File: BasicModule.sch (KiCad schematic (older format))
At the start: 12 parts, among them P1 CONN_01X03, Q1 Q_NPN_BCE, SW1 SW_Push_Dual

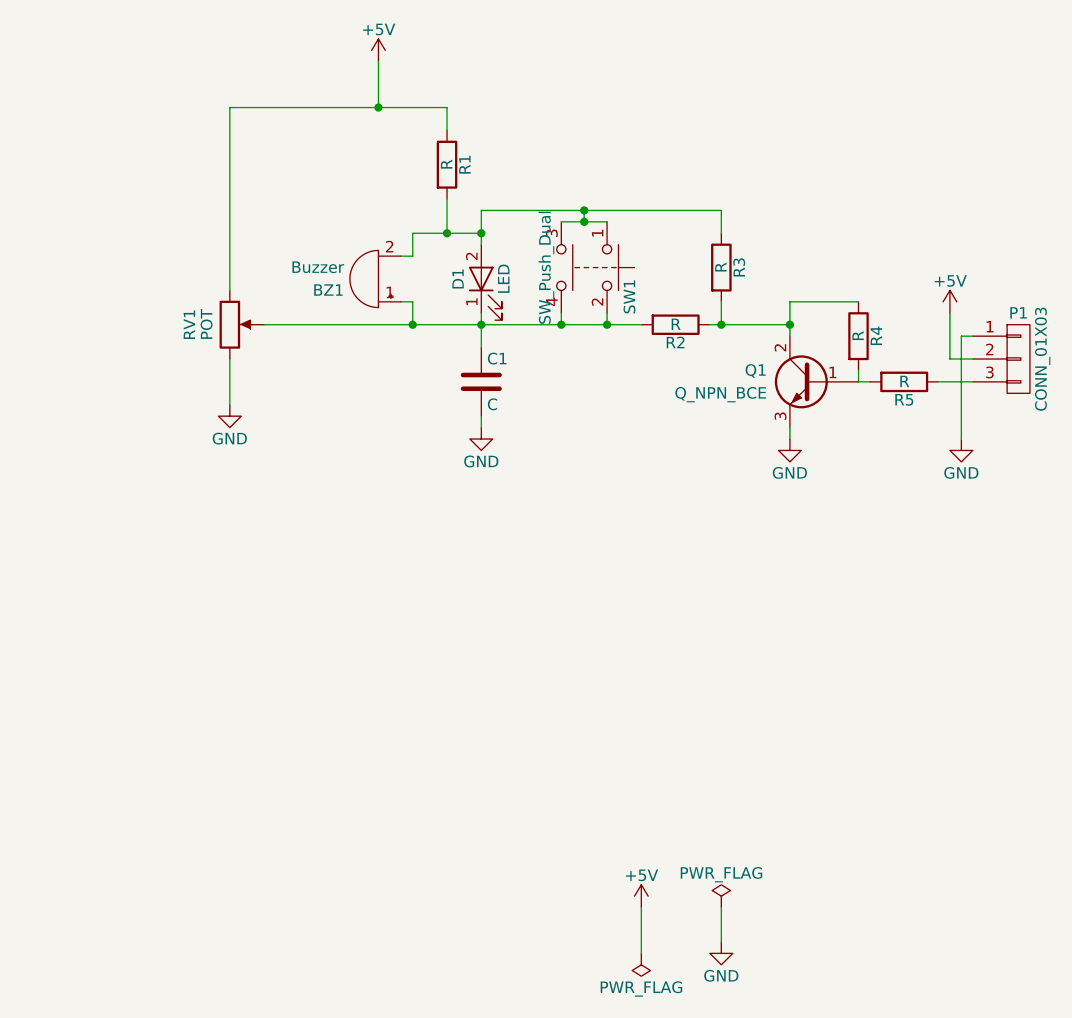
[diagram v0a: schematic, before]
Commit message: Se decide implementar el modulo solo para leds, buzzers y potenciometro
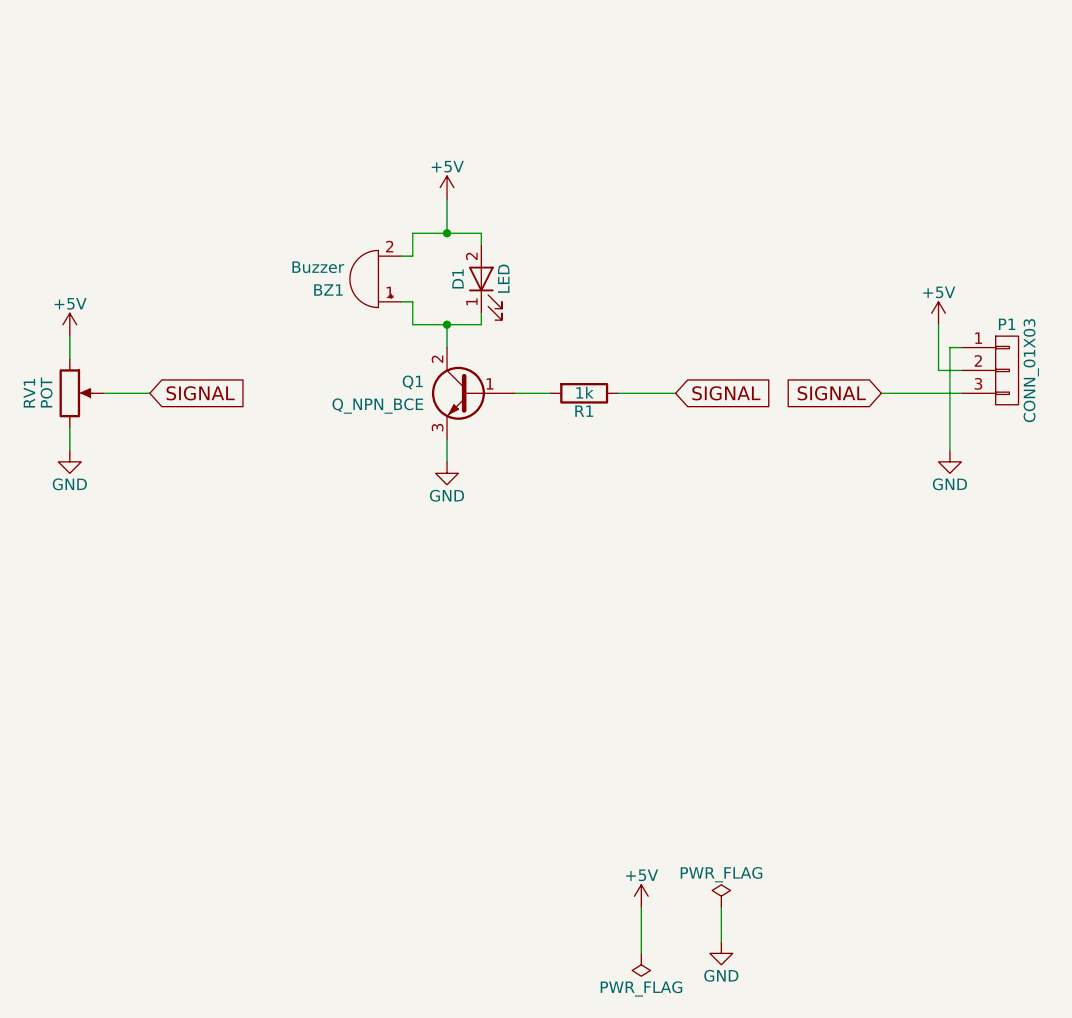
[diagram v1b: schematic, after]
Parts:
- removed C1: C, symbol C
- removed R2, R3, R4, R5: R, symbol R
- removed SW1: SW_Push_Dual, symbol SW_Push_Dual
- BZ1: footprint (none) -> Buzzers_Beepers:Buzzer_12x9.5RM7.6
- D1: footprint (none) -> LEDs:LED-5MM
- P1: footprint (none) -> Connectors_JST:JST_PH_S3B-PH-K_03x2.00mm_Angled
- Q1: footprint (none) -> TO_SOT_Packages_SMD:SOT-23
- R1: value R -> 1k; footprint (none) -> Resistors_SMD:R_0805
- RV1: footprint (none) -> w_pth_resistors:trimmer_alps-rk09k1130ah1
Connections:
- net +5V: now also BZ1.2 (+), D1.2 (A); no longer R1.1
- net at BZ1.1 (-), D1.1 (K): now also Q1.2 (C); no longer RV1.2
- net at Q1.1 (B): now also R1.2
- net SIGNAL: now reaches P1.3 (P3)
- net SIGNAL: now also R1.1, RV1.2
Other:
- moved on the sheet: P1, Q1, R1, RV1

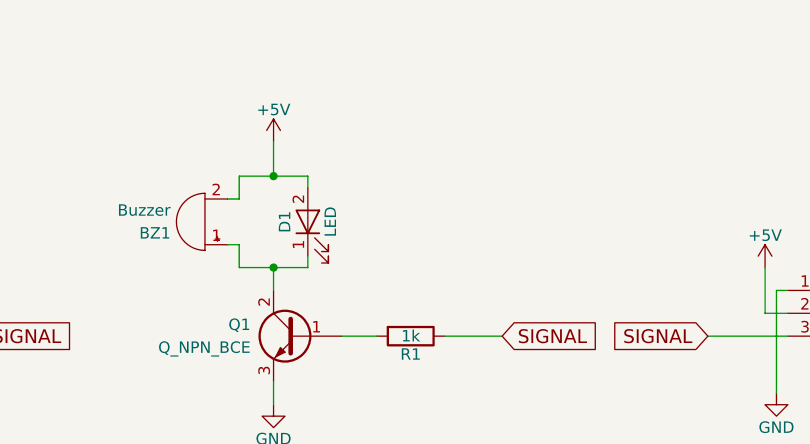
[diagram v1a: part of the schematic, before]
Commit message: Led piraña añadido al modulo
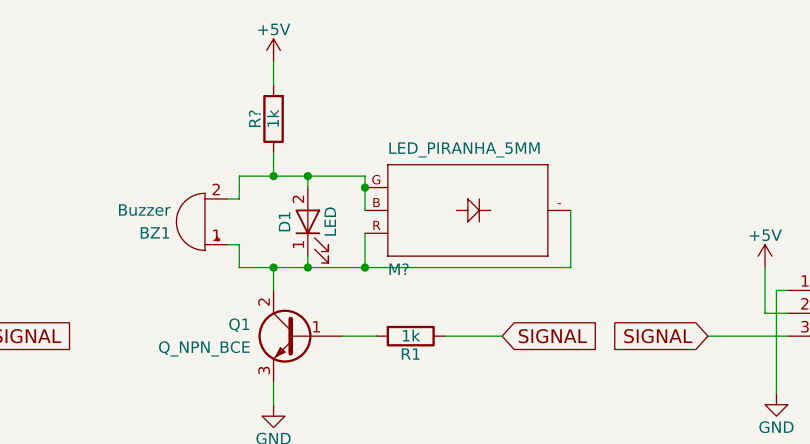
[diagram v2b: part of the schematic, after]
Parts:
- added M?: LED_PIRANHA_5MM, LED_PIRANHA_5MM, symbol LED_PIRANHA_5MM
- added R?: 1k, Resistors_SMD:R_0805, symbol R
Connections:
- net +5V: now also R?.2; no longer BZ1.2 (+), D1.2 (A)
- net at BZ1.1 (-), D1.1 (K), Q1.2 (C): now also M?.- (C), M?.R (RED)
- new net: BZ1.2 (+), D1.2 (A), M?.B (BLU), M?.G (GRN), R?.1
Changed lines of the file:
@@
 LIBS:рэс-49
 LIBS:тпг-1
+LIBS:SparkFun-LED
 LIBS:BasicModule-cache
 EELAYER 25 0
@@
 L +5V #PWR02
 U 1 1 5907709F
-P 5350 3950
-F 0 "#PWR02" H 5350 3800 50  0001 C CNN
-F 1 "+5V" H 5350 4090 50  0000 C CNN
-F 2 "" H 5350 3950 50  0001 C CNN
-F 3 "" H 5350 3950 50  0001 C CNN
-	1    5350 3950
+P 5350 3600
+F 0 "#PWR02" H 5350 3450 50  0001 C CNN
+F 1 "+5V" H 5350 3740 50  0000 C CNN
+F 2 "" H 5350 3600 50  0001 C CNN
+F 3 "" H 5350 3600 50  0001 C CNN
+	1    5350 3600
 	1    0    0    -1
 $EndComp
@@
 	5200 4200 5200 4100
 $Comp
-L +5V #PWR05
+L +5V #PWR03
 U 1 1 59078247
 P 7500 4500
-F 0 "#PWR05" H 7500 4350 50  0001 C CNN
+F 0 "#PWR03" H 7500 4350 50  0001 C CNN
 F 1 "+5V" H 7500 4640 50  0000 C CNN
 F 2 "" H 7500 4500 50  0001 C CNN
@@
 	7500 4700 7500 4500
 $Comp
-L GND #PWR06
+L GND #PWR04
 U 1 1 59078352
 P 7550 5050
-F 0 "#PWR06" H 7550 4800 50  0001 C CNN
+F 0 "#PWR04" H 7550 4800 50  0001 C CNN
 F 1 "GND" H 7550 4900 50  0000 C CNN
 F 2 "" H 7550 5050 50  0001 C CNN
@@
 	7550 4600 7550 5050
 $Comp
-L PWR_FLAG #FLG07
+L PWR_FLAG #FLG05
 U 1 1 590785A3
 P 6550 7050
-F 0 "#FLG07" H 6550 7125 50  0001 C CNN
+F 0 "#FLG05" H 6550 7125 50  0001 C CNN
 F 1 "PWR_FLAG" H 6550 7200 50  0000 C CNN
 F 2 "" H 6550 7050 50  0001 C CNN
@@
 $EndComp
 $Comp
-L GND #PWR08
+L GND #PWR06
 U 1 1 590786A5
 P 6550 7200
-F 0 "#PWR08" H 6550 6950 50  0001 C CNN
+F 0 "#PWR06" H 6550 6950 50  0001 C CNN
 F 1 "GND" H 6550 7050 50  0000 C CNN
 F 2 "" H 6550 7200 50  0001 C CNN
@@
 	6550 7050 6550 7200
 $Comp
-L +5V #PWR09
+L +5V #PWR07
 U 1 1 59078AD8
 P 6200 7050
-F 0 "#PWR09" H 6200 6900 50  0001 C CNN
+F 0 "#PWR07" H 6200 6900 50  0001 C CNN
 F 1 "+5V" H 6200 7190 50  0000 C CNN
 F 2 "" H 6200 7050 50  0001 C CNN
@@
 $EndComp
 $Comp
-L PWR_FLAG #FLG010
+L PWR_FLAG #FLG08
 U 1 1 59078BDF
 P 6200 7250
-F 0 "#FLG010" H 6200 7325 50  0001 C CNN
+F 0 "#FLG08" H 6200 7325 50  0001 C CNN
 F 1 "PWR_FLAG" H 6200 7400 50  0000 C CNN
 F 2 "" H 6200 7250 50  0001 C CNN
@@
 	5500 4100 5500 4150
 Wire Wire Line
-	5200 4500 5500 4500
+	5200 4500 6650 4500
 Wire Wire Line
 	5500 4500 5500 4450
@@
 	5350 5000 5350 5100
 Wire Wire Line
-	5200 4100 5500 4100
-Wire Wire Line
-	5350 3950 5350 4100
+	5200 4100 5750 4100
 Connection ~ 5350 4100
 Wire Wire Line
@@
 SIGNAL
 $Comp
-L +5V #PWR?
+L +5V #PWR09
 U 1 1 59109538
 P 3700 4550
-F 0 "#PWR?" H 3700 4400 50  0001 C CNN
+F 0 "#PWR09" H 3700 4400 50  0001 C CNN
 F 1 "+5V" H 3700 4690 50  0000 C CNN
 F 2 "" H 3700 4550 50  0001 C CNN
@@
 $EndComp
 $Comp
-L GND #PWR?
+L GND #PWR010
 U 1 1 591095BB
 P 3700 5050
-F 0 "#PWR?" H 3700 4800 50  0001 C CNN
+F 0 "#PWR010" H 3700 4800 50  0001 C CNN
 F 1 "GND" H 3700 4900 50  0000 C CNN
 F 2 "" H 3700 5050 50  0001 C CNN
@@
 Wire Wire Line
 	3700 4950 3700 5050
+$Comp
+L LED_PIRANHA_5MM M?
+U 1 1 5910A2C3
+P 6150 4250
+F 0 "M?" H 5850 4480 50  0000 L BNN
+F 1 "LED_PIRANHA_5MM" H 5850 3950 50  0000 L BNN
+F 2 "LED_PIRANHA_5MM" H 6180 4400 20  0001 C CNN
+F 3 "" H 6150 4250 60  0001 C CNN
+	1    6150 4250
+	1    0    0    1
+$EndComp
+$Comp
+L R R?
+U 1 1 5910A539
+P 5350 3850
+F 0 "R?" V 5430 3850 50  0000 C CNN
+F 1 "1k" V 5350 3850 50  0000 C CNN
+F 2 "Resistors_SMD:R_0805" V 5280 3850 50  0001 C CNN
+F 3 "" H 5350 3850 50  0001 C CNN
+	1    5350 3850
+	-1   0    0    1
+$EndComp
+Wire Wire Line
+	5350 3600 5350 3700
+Wire Wire Line
+	5350 4000 5350 4100
+Wire Wire Line
+	5750 4100 5750 4250
+Connection ~ 5500 4100
+Connection ~ 5750 4150
+Wire Wire Line
+	5750 4500 5750 4350
+Connection ~ 5500 4500
+Wire Wire Line
+	6650 4500 6650 4250
+Connection ~ 5750 4500
 $EndSCHEMATC

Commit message: Gerbers exportados
Gerbers exportados para prueba de panelizacion
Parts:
- M1: renamed from M?; footprint LED_PIRANHA_5MM -> SparkFun-LED:LED_PIRANHA_5MM
- gave numbers to parts that had none: 1
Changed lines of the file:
@@
 	3700 4950 3700 5050
 $Comp
-L LED_PIRANHA_5MM M?
+L LED_PIRANHA_5MM M1
 U 1 1 5910A2C3
 P 6150 4250
-F 0 "M?" H 5850 4480 50  0000 L BNN
+F 0 "M1" H 5850 4480 50  0000 L BNN
 F 1 "LED_PIRANHA_5MM" H 5850 3950 50  0000 L BNN
-F 2 "LED_PIRANHA_5MM" H 6180 4400 20  0001 C CNN
+F 2 "SparkFun-LED:LED_PIRANHA_5MM" H 6180 4400 20  0001 C CNN
 F 3 "" H 6150 4250 60  0001 C CNN
 	1    6150 4250
@@
 $EndComp
 $Comp
-L R R?
+L R R2
 U 1 1 5910A539
 P 5350 3850
-F 0 "R?" V 5430 3850 50  0000 C CNN
+F 0 "R2" V 5430 3850 50  0000 C CNN
 F 1 "1k" V 5350 3850 50  0000 C CNN
 F 2 "Resistors_SMD:R_0805" V 5280 3850 50  0001 C CNN

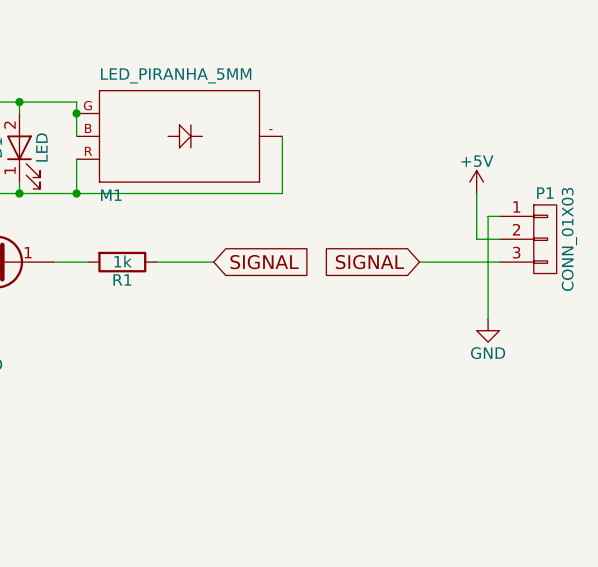
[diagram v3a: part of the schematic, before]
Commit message: Conector cambiado
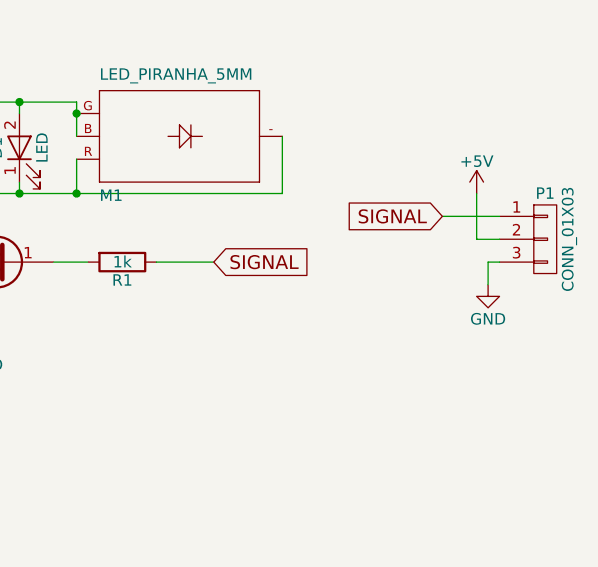
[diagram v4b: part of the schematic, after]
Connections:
- net GND: now also P1.3 (P3); no longer P1.1 (P1)
- net SIGNAL: now also P1.1 (P1); no longer P1.3 (P3)
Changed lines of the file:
@@
 EESchema Schematic File Version 2
-LIBS:power
-LIBS:device
-LIBS:transistors
-LIBS:conn
-LIBS:linear
-LIBS:regul
-LIBS:74xx
-LIBS:cmos4000
-LIBS:adc-dac
-LIBS:memory
-LIBS:xilinx
-LIBS:microcontrollers
-LIBS:dsp
-LIBS:microchip
-LIBS:analog_switches
-LIBS:motorola
-LIBS:texas
-LIBS:intel
-LIBS:audio
-LIBS:interface
-LIBS:digital-audio
-LIBS:philips
-LIBS:display
-LIBS:cypress
-LIBS:siliconi
-LIBS:opto
-LIBS:atmel
-LIBS:contrib
-LIBS:valves
-LIBS:74xgxx
-LIBS:5050_ws2811
-LIBS:a4988-module
-LIBS:ac-dc
-LIBS:acs712
-LIBS:actel
-LIBS:adxl345
-LIBS:allegro
-LIBS:Altera
-LIBS:AMS1117
-LIBS:analog_devices
-LIBS:ant
-LIBS:at24c64
-LIBS:battery_management
-LIBS:bbd
-LIBS:bc56-12EWA
-LIBS:bosch
-LIBS:brooktre
-LIBS:cmos_ieee
-LIBS:cp2103
-LIBS:CP2102
-LIBS:dc-dc
-LIBS:dht11
-LIBS:diode
-LIBS:elec-unifil
-LIBS:ESD_Protection
-LIBS:esp8266-module
-LIBS:ESP32
-LIBS:fe
-LIBS:ftdi
-LIBS:Gajda_opto
-LIBS:gennum
-LIBS:graphic
-LIBS:GS6300
-LIBS:gy-a4988_module
-LIBS:hc11
-LIBS:hc541
-LIBS:hc-05
-LIBS:HC164
-LIBS:hlk-rm04
-LIBS:ir
-LIBS:irf7907
-LIBS:isp_6p
-LIBS:l298n
-LIBS:Lattice
-LIBS:LM2575
-LIBS:logo
-LIBS:logo-azura-wrench
-LIBS:M25P05
-LIBS:max1538
-LIBS:maxim
-LIBS:mcp1640
-LIBS:mcp1640b
-LIBS:MCP3208
-LIBS:mechanical
-LIBS:microchip_dspic33dsc
-LIBS:microchip_pic10mcu
-LIBS:microchip_pic12mcu
-LIBS:microchip_pic16mcu
-LIBS:microchip_pic18mcu
-LIBS:microchip_pic32mcu
-LIBS:miniusb
-LIBS:motor_drivers
-LIBS:motors
-LIBS:mp2109dq
-LIBS:MP2307DN
-LIBS:msp430
-LIBS:na10-psu
-LIBS:nordicsemi
-LIBS:nrf24l01
-LIBS:nxp_armmcu
-LIBS:OF5032
-LIBS:onsemi
-LIBS:Oscillators
-LIBS:pl2303
-LIBS:pogopin
-LIBS:powerint
-LIBS:powerjack
-LIBS:Power_Management
-LIBS:pspice
-LIBS:pt4115
-LIBS:references
-LIBS:relays
-LIBS:rfcom
-LIBS:RJ45-ENCODER
-LIBS:rtl8196
-LIBS:sensors
-LIBS:silabs
-LIBS:smd oscillator
-LIBS:songle_relay
-LIBS:spiflash_16m
-LIBS:st1s10
-LIBS:stc12c5a60s2
-LIBS:stepper_drivers
-LIBS:stm8
-LIBS:stm32
-LIBS:STM32F100RBT6B
-LIBS:stpdn
-LIBS:supertex
-LIBS:switches
-LIBS:tcs3200d
-LIBS:tda5144
-LIBS:test
-LIBS:texas-msp
-LIBS:tp4056
-LIBS:transf
-LIBS:ts812c
-LIBS:ttl_ieee
-LIBS:usb_a
-LIBS:usb-a-pcb
-LIBS:usb_ax2
-LIBS:video
-LIBS:wiznet
-LIBS:Worldsemi
-LIBS:ws2812
-LIBS:xc3s100etq144
-LIBS:xc3s500evq100
-LIBS:xc6slx9-tqg144
-LIBS:XC9572-TQ100
-LIBS:Xicor
-LIBS:xilinx_spartan3_virtex4_and_5
-LIBS:zetex
-LIBS:Zilog
-LIBS:рэс-49
-LIBS:тпг-1
 LIBS:SparkFun-LED
 LIBS:BasicModule-cache
@@
 L GND #PWR04
 U 1 1 59078352
-P 7550 5050
-F 0 "#PWR04" H 7550 4800 50  0001 C CNN
-F 1 "GND" H 7550 4900 50  0000 C CNN
-F 2 "" H 7550 5050 50  0001 C CNN
-F 3 "" H 7550 5050 50  0001 C CNN
-	1    7550 5050
-	1    0    0    -1
-$EndComp
-Wire Wire Line
-	7600 4600 7550 4600
-Wire Wire Line
-	7550 4600 7550 5050
+P 7550 4900
+F 0 "#PWR04" H 7550 4650 50  0001 C CNN
+F 1 "GND" H 7550 4750 50  0000 C CNN
+F 2 "" H 7550 4900 50  0001 C CNN
+F 3 "" H 7550 4900 50  0001 C CNN
+	1    7550 4900
+	1    0    0    -1
+$EndComp
 $Comp
 L PWR_FLAG #FLG05
@@
 Text GLabel 6350 4800 2    60   Input ~ 0
 SIGNAL
-Wire Wire Line
-	7600 4800 7250 4800
-Text GLabel 7250 4800 0    60   Input ~ 0
+Text GLabel 7350 4600 0    60   Input ~ 0
 SIGNAL
 $Comp
@@
 	6650 4500 6650 4250
 Connection ~ 5750 4500
+Wire Wire Line
+	7350 4600 7600 4600
+Wire Wire Line
+	7600 4800 7550 4800
+Wire Wire Line
+	7550 4800 7550 4900
 $EndSCHEMATC

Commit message: arbol de carpetas cambiado
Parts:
- BZ1: footprint Buzzers_Beepers:Buzzer_12x9.5RM7.6 -> lib_fp:Buzzer_12x9.5RM7.6
- D1: footprint LEDs:LED-5MM -> lib_fp:LED-5MM
- M1: footprint SparkFun-LED:LED_PIRANHA_5MM -> lib_fp:LED_PIRANHA_5MM
- P1: footprint Connectors_JST:JST_PH_S3B-PH-K_03x2.00mm_Angled -> lib_fp:JST_PH_S3B-PH-K_03x2.00mm_Angled
- Q1: footprint TO_SOT_Packages_SMD:SOT-23 -> lib_fp:SOT-23
- R1, R2: footprint Resistors_SMD:R_0805 -> lib_fp:R_0805
- RV1: footprint w_pth_resistors:trimmer_alps-rk09k1130ah1 -> lib_fp:trimmer_alps-rk09k1130ah1
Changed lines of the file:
@@
 EESchema Schematic File Version 2
-LIBS:SparkFun-LED
-LIBS:BasicModule-cache
+LIBS:BasicModule
 EELAYER 25 0
 EELAYER END
@@
 encoding utf-8
 Sheet 1 1
-Title ""
-Date ""
-Rev ""
-Comp ""
-Comment1 ""
+Title "Modulo basico I"
+Date "2018-03-04"
+Rev "v1.0"
+Comp "Frizzy Electronics"
+Comment1 "David Matias"
 Comment2 ""
 Comment3 ""
@@
 F 0 "RV1" V 3525 4800 50  0000 C CNN
 F 1 "POT" V 3600 4800 50  0000 C CNN
-F 2 "w_pth_resistors:trimmer_alps-rk09k1130ah1" H 3700 4800 50  0001 C CNN
+F 2 "lib_fp:trimmer_alps-rk09k1130ah1" H 3700 4800 50  0001 C CNN
 F 3 "" H 3700 4800 50  0001 C CNN
 	1    3700 4800
@@
 F 0 "BZ1" H 5200 4350 50  0000 L CNN
 F 1 "Buzzer" H 5200 4250 50  0000 L CNN
-F 2 "Buzzers_Beepers:Buzzer_12x9.5RM7.6" V 5025 4400 50  0001 C CNN
+F 2 "lib_fp:Buzzer_12x9.5RM7.6" V 5025 4400 50  0001 C CNN
 F 3 "" V 5025 4400 50  0001 C CNN
 	1    5050 4300
@@
 F 0 "D1" H 5500 4400 50  0000 C CNN
 F 1 "LED" H 5500 4200 50  0000 C CNN
-F 2 "LEDs:LED-5MM" H 5500 4300 50  0001 C CNN
+F 2 "lib_fp:LED-5MM" H 5500 4300 50  0001 C CNN
 F 3 "" H 5500 4300 50  0001 C CNN
 	1    5500 4300
@@
 F 0 "Q1" H 5650 4850 50  0000 L CNN
 F 1 "Q_NPN_BCE" H 5650 4750 50  0000 L CNN
-F 2 "TO_SOT_Packages_SMD:SOT-23" H 5650 4900 50  0001 C CNN
+F 2 "lib_fp:SOT-23" H 5650 4900 50  0001 C CNN
 F 3 "" H 5450 4800 50  0001 C CNN
 	1    5450 4800
@@
 F 0 "R1" V 6030 4800 50  0000 C CNN
 F 1 "1k" V 5950 4800 50  0000 C CNN
-F 2 "Resistors_SMD:R_0805" V 5880 4800 50  0001 C CNN
+F 2 "lib_fp:R_0805" V 5880 4800 50  0001 C CNN
 F 3 "" H 5950 4800 50  0001 C CNN
 	1    5950 4800
@@
 F 0 "P1" H 7800 4900 50  0000 C CNN
 F 1 "CONN_01X03" V 7900 4700 50  0000 C CNN
-F 2 "Connectors_JST:JST_PH_S3B-PH-K_03x2.00mm_Angled" H 7800 4700 50  0001 C CNN
+F 2 "lib_fp:JST_PH_S3B-PH-K_03x2.00mm_Angled" H 7800 4700 50  0001 C CNN
 F 3 "" H 7800 4700 50  0001 C CNN
 	1    7800 4700
@@
 F 0 "M1" H 5850 4480 50  0000 L BNN
 F 1 "LED_PIRANHA_5MM" H 5850 3950 50  0000 L BNN
-F 2 "SparkFun-LED:LED_PIRANHA_5MM" H 6180 4400 20  0001 C CNN
+F 2 "lib_fp:LED_PIRANHA_5MM" H 6180 4400 20  0001 C CNN
 F 3 "" H 6150 4250 60  0001 C CNN
 	1    6150 4250
@@
 F 0 "R2" V 5430 3850 50  0000 C CNN
 F 1 "1k" V 5350 3850 50  0000 C CNN
-F 2 "Resistors_SMD:R_0805" V 5280 3850 50  0001 C CNN
+F 2 "lib_fp:R_0805" V 5280 3850 50  0001 C CNN
 F 3 "" H 5350 3850 50  0001 C CNN
 	1    5350 3850

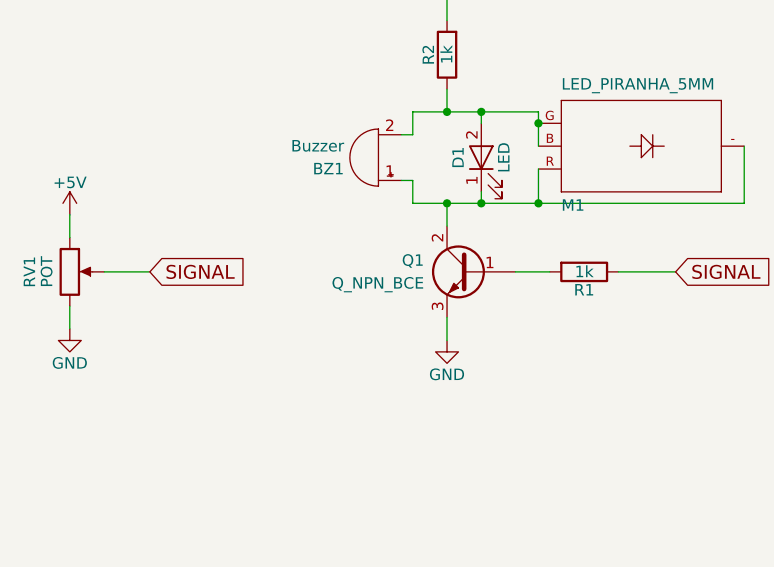
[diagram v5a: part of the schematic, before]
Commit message: Valor del transistor cambiado
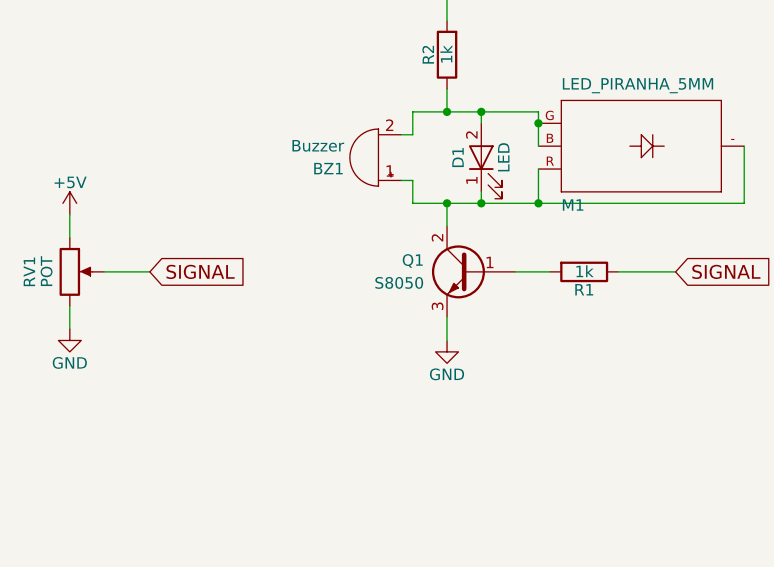
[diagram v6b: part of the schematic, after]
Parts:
- Q1: value Q_NPN_BCE -> S8050
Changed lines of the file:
@@
 EESchema Schematic File Version 2
 LIBS:BasicModule
+LIBS:BasicModule-cache
 EELAYER 25 0
 EELAYER END
@@
 P 5450 4800
 F 0 "Q1" H 5650 4850 50  0000 L CNN
-F 1 "Q_NPN_BCE" H 5650 4750 50  0000 L CNN
+F 1 "S8050" H 5650 4750 50  0000 L CNN
 F 2 "lib_fp:SOT-23" H 5650 4900 50  0001 C CNN
 F 3 "" H 5450 4800 50  0001 C CNN
